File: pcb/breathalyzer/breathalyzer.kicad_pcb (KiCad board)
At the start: 2 copper layers, 37 parts, among them IC1 TPS3840DL25DBVR, J1 Conn_01x07_Pin, J2 MP-3B socket, Q1 Q_PMOS, Q2 NPN, SW1 PTS636SK43SMTR, SW2 430162085826, U1 STM32F030K6Tx, U2 TLV73325PDBV, U4 TLV61070ADBV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

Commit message: update from schematic
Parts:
- removed the R1 at (127.1, 108.4)
- added RV1: 50k_Potentiometer, Potentiometer_THT:Potentiometer_ACP_CA9-H5_Horizontal, F.Cu at (124.5, 109.3)
- SW2: value 430162085826 -> SW_Push_Dual
- moved SW2 5.24 mm to (215.3, 114.3)
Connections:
- SW2 pad 2: (no net) -> unconnected-(SW2-Pad2)
- SW2 pad 4: (no net) -> unconnected-(SW2-Pad4)

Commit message: net classes
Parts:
- moved J1 114.8 mm to (144.8, 188.0)
- moved U5 103.1 mm to (188.0, 55.9)
- moved BZ1 61.4 mm to (129.5, 175.3)
- moved U4 30.6 mm to (143.7, 132.6)
- moved R7 30.6 mm to (138.4, 131.9)
- moved L2 30.6 mm to (148.8, 132.1)
- moved DS1 24.0 mm to (151.1, 41.8)
- moved C10 11.2 mm to (160.2, 131.4)
- moved C11 11.2 mm to (160.2, 134.4)
- moved C9 11.2 mm to (160.0, 137.2)
- moved R6 11.2 mm to (160.0, 139.7)
- moved U1 8.09 mm to (148.6, 85.5)
- moved C4 3.36 mm to (138.9, 86.4)
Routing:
- net +2V5: track 0.00 -> 0.56 mm
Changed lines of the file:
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@@
 	(footprint "Capacitor_SMD:C_0603_1608Metric"
 		(layer "F.Cu")
-		(at 140.89 89.09)
+		(at 138.925 86.36)
 		(descr "Capacitor SMD 0603 (1608 Metric), square (rectangular) end terminal, IPC-7351 nominal, (Body size source: IPC-SM-782 page 76, https://www.pcb-3d.com/wordpress/wp-content/uploads/ipc-sm-782a_amendment_1_and_2.pdf), generated with kicad-footprint-generator")
 		(tags "capacitor")
@@
 	(footprint "Package_LCC:PLCC-44"
 		(layer "F.Cu")
-		(at 147.915 150.86)
+		(at 187.96 55.88)
 		(descr "PLCC, 44 pins, surface mount")
 		(tags "plcc smt")
@@
 	(footprint "Resistor_SMD:R_1206_3216Metric"
 		(layer "F.Cu")
-		(at 140.895 162.34)
+		(at 138.355 131.86)
 		(descr "Resistor SMD 1206 (3216 Metric), square (rectangular) end terminal, IPC-7351 nominal, (Body size source: IPC-SM-782 page 72, https://www.pcb-3d.com/wordpress/wp-content/uploads/ipc-sm-782a_amendment_1_and_2.pdf), generated with kicad-footprint-generator")
 		(tags "resistor")
@@
 	(footprint "Capacitor_SMD:C_0805_2012Metric"
 		(layer "F.Cu")
-		(at 159.965 142.54)
+		(at 160.24 131.39)
 		(descr "Capacitor SMD 0805 (2012 Metric), square (rectangular) end terminal, IPC-7351 nominal, (Body size source: IPC-SM-782 page 76, https://www.pcb-3d.com/wordpress/wp-content/uploads/ipc-sm-782a_amendment_1_and_2.pdf, https://docs.google.com/spreadsheets/d/1BsfQQcO9C6DZCsRaXUlFlo91Tg2WpOkGARC1WS5S8t0/edit?usp=sharing), generated with kicad-footprint-generator")
 		(tags "capacitor")
@@
 	(footprint "Capacitor_SMD:C_0603_1608Metric"
 		(layer "F.Cu")
-		(at 159.745 148.31)
+		(at 160.02 137.16)
 		(descr "Capacitor SMD 0603 (1608 Metric), square (rectangular) end terminal, IPC-7351 nominal, (Body size source: IPC-SM-782 page 76, https://www.pcb-3d.com/wordpress/wp-content/uploads/ipc-sm-782a_amendment_1_and_2.pdf), generated with kicad-footprint-generator")
 		(tags "capacitor")
@@
 	(footprint "breathalyzer:HDRRA7W66P0X254_1X7_1778X229X274P"
 		(layer "F.Cu")
-		(at 193.04 83.82)
+		(at 144.78 187.96)
 		(descr "22-28-8073")
 		(tags "Connector")
@@
 	(footprint "Package_TO_SOT_SMD:SOT-23-6"
 		(layer "F.Cu")
-		(at 146.275 163.085)
+		(at 143.735 132.605)
 		(descr "SOT, 6 Pin (JEDEC MO-178 Var AB https://www.jedec.org/document_search?search_api_views_fulltext=MO-178), generated with kicad-footprint-generator ipc_gullwing_generator.py")
 		(tags "SOT TO_SOT_SMD")
@@
 	(footprint "Capacitor_SMD:C_0805_2012Metric"
 		(layer "F.Cu")
-		(at 159.965 145.55)
+		(at 160.24 134.4)
 		(descr "Capacitor SMD 0805 (2012 Metric), square (rectangular) end terminal, IPC-7351 nominal, (Body size source: IPC-SM-782 page 76, https://www.pcb-3d.com/wordpress/wp-content/uploads/ipc-sm-782a_amendment_1_and_2.pdf, https://docs.google.com/spreadsheets/d/1BsfQQcO9C6DZCsRaXUlFlo91Tg2WpOkGARC1WS5S8t0/edit?usp=sharing), generated with kicad-footprint-generator")
 		(tags "capacitor")
@@
 	(footprint "breathalyzer:CPT1414680T"
 		(layer "F.Cu")
-		(at 182.88 144.78)
+		(at 129.54 175.26)
 		(descr "CPT-14146-80T-2")
 		(tags "Inductor")
@@
 	(footprint "Package_QFP:LQFP-32_7x7mm_P0.8mm"
 		(layer "F.Cu")
-		(at 148.6 93.54)
+		(at 148.6 85.455)
 		(descr "LQFP, 32 Pin (https://www.nxp.com/docs/en/package-information/SOT358-1.pdf), generated with kicad-footprint-generator ipc_gullwing_generator.py")
 		(tags "LQFP QFP")
@@
 	(footprint "breathalyzer:LCD-S301C31TR"
 		(layer "F.Cu")
-		(at 163.83 62.07)
+		(at 151.13 41.75)
 		(descr "LCD-S301C31TR")
 		(tags "Display")
@@
 	(footprint "Resistor_SMD:R_0603_1608Metric"
 		(layer "F.Cu")
-		(at 159.745 150.82)
+		(at 160.02 139.67)
 		(descr "Resistor SMD 0603 (1608 Metric), square (rectangular) end terminal, IPC-7351 nominal, (Body size source: IPC-SM-782 page 72, https://www.pcb-3d.com/wordpress/wp-content/uploads/ipc-sm-782a_amendment_1_and_2.pdf), generated with kicad-footprint-generator")
 		(tags "resistor")
@@
 	(footprint "Inductor_SMD:L_1008_2520Metric"
 		(layer "F.Cu")
-		(at 151.325 162.56)
+		(at 148.785 132.08)
 		(descr "Inductor SMD 1008 (2520 Metric), square (rectangular) end terminal, IPC-7351 nominal, (Body size source: https://ecsxtal.com/store/pdf/ECS-MPI2520-SMD-POWER-INDUCTOR.pdf), generated with kicad-footprint-generator")
 		(tags "inductor")
@@
 		)
 	)
+	(segment
+		(start 144.425 82.655)
+		(end 144.980918 82.655)
+		(width 0.2)
+		(layer "F.Cu")
+		(net 3)
+	)
 	(embedded_fonts no)

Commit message: +5V
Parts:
- removed C6: 1 uF, Capacitor_SMD:C_0603_1608Metric
- removed C7: 10 uF, Capacitor_SMD:C_0805_2012Metric
- removed IC1: TPS3840DL25DBVR, Package_TO_SOT_SMD:SOT-23-5_HandSoldering
- removed L1: 24 nH, Inductor_SMD:L_1008_2520Metric
- removed R1: 100k, Resistor_SMD:R_0402_1005Metric
- removed the R2 at (140.9, 96.6)
- removed R3: 56k, Resistor_SMD:R_0603_1608Metric
- removed the R4 at (138.2, 78.7)
- moved U2 72.4 mm to (208.1, 141.3)
- moved R7 56.2 mm to (193.0, 144.8), turned to -90 degrees
- moved U4 45.5 mm to (188.1, 142.6)
- moved L2 42.4 mm to (190.7, 138.4)
- moved R8 37.4 mm to (177.8, 151.1), turned to 180 degrees
- moved Q1 35.9 mm to (184.3, 151.1), turned to 90 degrees
- moved R6 32.1 mm to (190.5, 149.9)
- moved BT1 30.8 mm to (179.1, 147.3)
- moved C3 21.2 mm to (141.4, 82.5), turned to 180 degrees
- moved C1 18.5 mm to (142.0, 86.4), turned to 180 degrees
- moved C2 13.0 mm to (155.7, 88.9)
- moved R4 4.38 mm to (193.5, 122.0)
- moved R5 4.38 mm to (193.5, 124.5)
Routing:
- net +BATT: track 0.00 -> 24.7 mm
- net Net-(U4-V_{FB}): track 0.00 -> 9.27 mm
- net +2V5: track 0.56 -> 7.50 mm
- net Net-(U4-SW): track 0.00 -> 6.88 mm, vias 0 -> 2
- net Net-(BT1-+): track 0.00 -> 6.32 mm
- net Net-(Q1-G): track 0.00 -> 5.18 mm
- net +5V: track 0.00 -> 4.12 mm
- net GND: track 0.00 -> 3.85 mm

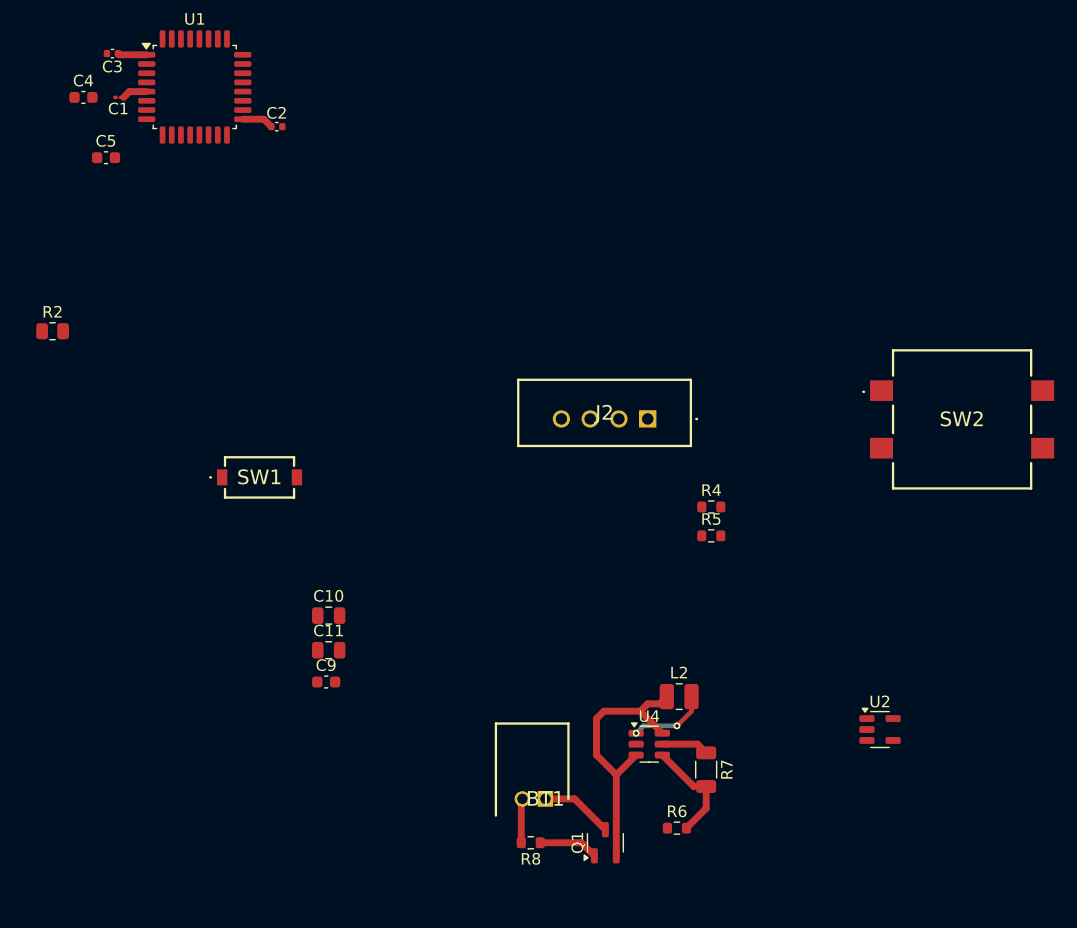
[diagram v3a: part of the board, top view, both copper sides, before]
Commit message: 5V fix
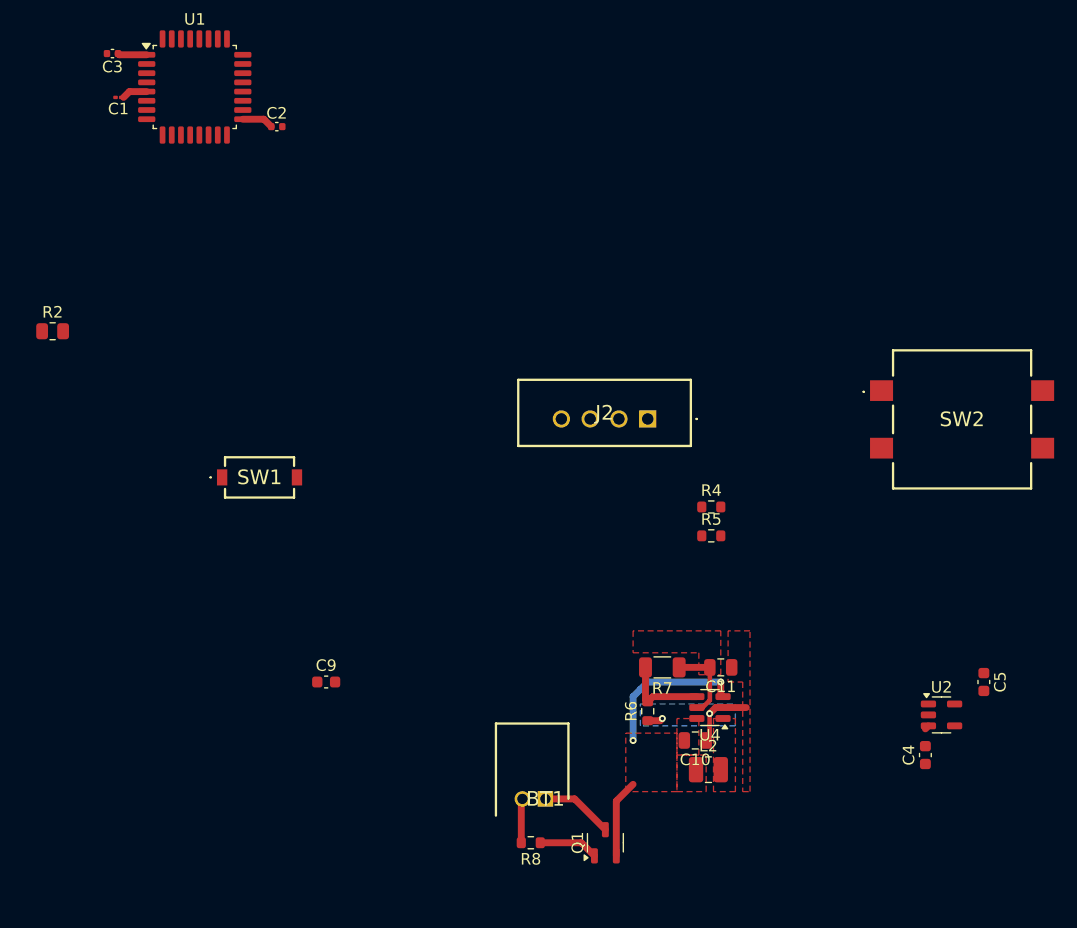
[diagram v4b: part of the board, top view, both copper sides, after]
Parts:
- moved C4 92.8 mm to (212.1, 143.5), turned to 90 degrees
- moved C5 88.9 mm to (217.2, 137.2), turned to -90 degrees
- moved C11 34.1 mm to (194.3, 135.9), turned to 180 degrees
- moved C10 33.6 mm to (192.1, 142.2), turned to 180 degrees
- moved R6 10.5 mm to (188.0, 139.7), turned to 90 degrees
- moved R7 9.67 mm to (189.2, 135.9), turned to 180 degrees
- moved L2 6.84 mm to (193.2, 144.8)
- moved U4 6.16 mm to (193.4, 139.4), turned to 180 degrees
- moved U2 5.49 mm to (213.5, 140.0)
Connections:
- C11 pad 1: Net-(U4-V_{FB}) -> GND
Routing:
- net GND: track 3.85 -> 11.1 mm, vias 0 -> 2
- net Net-(U4-SW): track 6.88 -> 0.00 mm, vias 2 -> 0
- net +BATT: track 24.7 -> 20.1 mm, vias 0 -> 2
- net +5V: track 4.12 -> 7.79 mm
- net Net-(U4-V_{FB}): track 9.27 -> 7.52 mm
- added copper zone on F.Cu, net +5V
- added copper zone on F.Cu, net +BATT
- added copper zone on B.Cu, net GND
- added copper zone on F.Cu, net GND
- added copper zone on F.Cu, net Net-(U4-SW)

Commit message: +2V5
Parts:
- moved C4 35.2 mm to (177.8, 135.8)
- moved C5 33.1 mm to (184.2, 135.8), turned to 90 degrees
- moved U2 32.6 mm to (181.1, 136.2)
- moved R4 23.8 mm to (169.7, 122.6)
- moved R5 23.8 mm to (169.7, 125.1)
- moved BT1 4.84 mm to (181.0, 142.9), turned to 90 degrees
- moved R8 3.17 mm to (180.3, 149.2), turned to 90 degrees
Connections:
- U2 pad 4: unconnected-(U2-NC-Pad4) -> GND
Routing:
- net +5V: track 7.79 -> 28.3 mm, vias 0 -> 2
- net Net-(BT1-+): track 6.32 -> 8.49 mm
- net Net-(Q1-G): track 5.18 -> 3.91 mm
- added copper zone on F.Cu, net +2V5

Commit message: pcb layout
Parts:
- BT1, BZ1, C1, C10, C11, C2, C3, C4, C5, J1, J2, L2, Q1, Q2, R2, R4, R5, R6, R7, R8, SW1, U1, U2, U4: moved to B.Cu
- moved BZ1 114.8 mm to (140.3, 61.0), turned to 180 degrees
- moved Q2 85.6 mm to (137.3, 41.9)
- moved J2 81.3 mm to (152.3, 41.3)
- moved J1 78.8 mm to (141.0, 109.2)
- moved Q1 71.9 mm to (138.4, 95.8), turned to -90 degrees
- moved R8 69.0 mm to (134.4, 97.7), turned to -90 degrees
- moved SW2 68.3 mm to (148.6, 99.7)
- moved RV1 62.9 mm to (155.7, 54.6)
- moved R2 62.6 mm to (133.3, 44.2), turned to -90 degrees
- moved L2 62.0 mm to (153.0, 97.6), turned to 90 degrees
- moved C9 59.2 mm to (136.1, 82.9)
- moved BT1 57.1 mm to (139.1, 104.0), turned to -90 degrees
- moved C10 56.8 mm to (155.6, 98.7), turned to -90 degrees
- moved R5 56.2 mm to (151.8, 71.8)
- moved U4 54.6 mm to (158.4, 97.5), turned to -90 degrees
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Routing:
- net LCD_A1: track 0.00 -> 57.1 mm
- net LCD_B1: track 0.00 -> 55.3 mm
- net LCD_G3: track 0.00 -> 48.5 mm
- net LCD_F1: track 0.00 -> 43.2 mm, vias 0 -> 1
- net LCD_F3: track 0.00 -> 42.1 mm
- net LCD_G2: track 0.00 -> 39.5 mm
- net LCD_F2: track 0.00 -> 35.9 mm
- net LCD_G1: track 0.00 -> 33.8 mm, vias 0 -> 1
- net ADC_IN: track 0.00 -> 33.3 mm, vias 0 -> 1
- net LCD_B3: track 0.00 -> 30.6 mm, vias 0 -> 1
- net LCD_B2: track 0.00 -> 30.6 mm
- net LCD_A3: track 0.00 -> 30.1 mm
- net LCD_A2: track 0.00 -> 30.1 mm
- net LCD_C1: track 0.00 -> 26.6 mm, vias 0 -> 1
- net LCD_E1: track 0.00 -> 26.4 mm, vias 0 -> 1
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- added copper zone on B.Cu, net +2V5
- added copper zone on B.Cu, net +5V
- added copper zone on B.Cu, net +BATT
- added copper zone on B.Cu, net Net-(U4-SW)
- removed copper zone on F.Cu, net +2V5
- removed copper zone on F.Cu, net +5V
- removed copper zone on F.Cu, net +BATT
- removed copper zone on F.Cu, net Net-(U4-SW)

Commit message: layout update
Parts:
- RV1: moved to B.Cu
- moved BZ1 60.6 mm to (158.8, 118.7)
- moved RV1 30.7 mm to (163.2, 84.5), turned to 180 degrees
- moved SW1 29.0 mm to (161.9, 74.9)
- moved C4 12.8 mm to (159.5, 100.5)
- moved C5 12.8 mm to (159.5, 94.2)
- moved U2 12.8 mm to (159.1, 97.2)
- moved C11 9.54 mm to (152.4, 96.1)
- moved L2 9.54 mm to (143.5, 97.2)
- moved R6 9.54 mm to (148.6, 102.4)
- moved R7 9.54 mm to (152.4, 101.2)
- moved U4 9.54 mm to (148.9, 97.0)
- moved C10 9.54 mm to (146.1, 98.3)
- moved J1 6.99 mm to (134.0, 109.2)
- moved BT1 1.08 mm to (139.1, 102.9)
- moved Q1 1.08 mm to (138.4, 94.7)
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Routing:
- net +5V: track 28.3 -> 7.41 mm, vias 2 -> 0

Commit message: layout update
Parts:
- moved C2 21.1 mm to (154.4, 53.9)
- moved R4 21.1 mm to (145.1, 64.1)
- moved C1 21.1 mm to (140.6, 56.5)
- moved C3 21.1 mm to (140.1, 60.3)
- moved U1 21.1 mm to (147.2, 57.4)
- moved R5 21.1 mm to (150.2, 50.8)
- moved SW1 1.83 mm to (161.9, 76.8)
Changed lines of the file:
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@@
 	(footprint "Resistor_SMD:R_0603_1608Metric"
 		(layer "B.Cu")
-		(at 146.735 85.185 180)
+		(at 145.135 64.1 180)
 		(descr "Resistor SMD 0603 (1608 Metric), square (rectangular) end terminal, IPC-7351 nominal, (Body size source: IPC-SM-782 page 72, https://www.pcb-3d.com/wordpress/wp-content/uploads/ipc-sm-782a_amendment_1_and_2.pdf), generated with kicad-footprint-generator")
 		(tags "resistor")
@@
 	(footprint "Capacitor_SMD:C_0402_1005Metric"
 		(layer "B.Cu")
-		(at 141.675 81.375 180)
+		(at 140.075 60.29 180)
 		(descr "Capacitor SMD 0402 (1005 Metric), square (rectangular) end terminal, IPC-7351 nominal, (Body size source: IPC-SM-782 page 76, https://www.pcb-3d.com/wordpress/wp-content/uploads/ipc-sm-782a_amendment_1_and_2.pdf), generated with kicad-footprint-generator")
 		(tags "capacitor")
@@
 	(footprint "Capacitor_SMD:C_0402_1005Metric"
 		(layer "B.Cu")
-		(at 155.955 75.025)
+		(at 154.355 53.94)
 		(descr "Capacitor SMD 0402 (1005 Metric), square (rectangular) end terminal, IPC-7351 nominal, (Body size source: IPC-SM-782 page 76, https://www.pcb-3d.com/wordpress/wp-content/uploads/ipc-sm-782a_amendment_1_and_2.pdf), generated with kicad-footprint-generator")
 		(tags "capacitor")
@@
 	(footprint "breathalyzer:PTS636SM43JSMTRLFS"
 		(layer "B.Cu")
-		(at 161.925 74.93 -90)
+		(at 161.925 76.76 -90)
 		(descr "PTS636SM43JSMTR LFS-1")
 		(tags "Switch")
@@
 	(footprint "Resistor_SMD:R_0603_1608Metric"
 		(layer "B.Cu")
-		(at 151.815 71.85)
+		(at 150.215 50.765)
 		(descr "Resistor SMD 0603 (1608 Metric), square (rectangular) end terminal, IPC-7351 nominal, (Body size source: IPC-SM-782 page 72, https://www.pcb-3d.com/wordpress/wp-content/uploads/ipc-sm-782a_amendment_1_and_2.pdf), generated with kicad-footprint-generator")
 		(tags "resistor")
@@
 	(footprint "Package_QFP:LQFP-32_7x7mm_P0.8mm"
 		(layer "B.Cu")
-		(at 148.825 78.47)
+		(at 147.225 57.385)
 		(descr "LQFP, 32 Pin (https://www.nxp.com/docs/en/package-information/SOT358-1.pdf), generated with kicad-footprint-generator ipc_gullwing_generator.py")
 		(tags "LQFP QFP")
@@
 	(footprint "Capacitor_SMD:C_01005_0402Metric"
 		(layer "B.Cu")
-		(at 142.19 77.565 180)
+		(at 140.59 56.48 180)
 		(descr "Capacitor SMD 01005 (0402 Metric), square (rectangular) end terminal, IPC-7351 nominal, (Body size source: http://www.vishay.com/docs/20056/crcw01005e3.pdf), generated with kicad-footprint-generator")
 		(tags "capacitor")
@@
 	)
 	(segment
-		(start 152.64 73.28)
-		(end 151.625 74.295)
+		(start 151.04 52.195)
+		(end 150.025 53.21)
 		(width 0.6)
 		(layer "B.Cu")
@@
 	)
 	(segment
-		(start 152.64 71.85)
-		(end 152.64 73.28)
+		(start 151.04 50.765)
+		(end 151.04 52.195)
 		(width 0.6)
 		(layer "B.Cu")
@@
 	)
 	(segment
-		(start 145.91 82.76)
-		(end 146.025 82.645)
+		(start 144.31 61.675)
+		(end 144.425 61.56)
 		(width 0.6)
 		(layer "B.Cu")
@@
 	)
 	(segment
-		(start 145.91 85.185)
-		(end 145.91 82.76)
+		(start 144.31 64.1)
+		(end 144.31 61.675)
 		(width 0.6)
 		(layer "B.Cu")
@@
 	)
 	(segment
-		(start 153 75.67)
-		(end 154.83 75.67)
+		(start 151.4 54.585)
+		(end 153.23 54.585)
 		(width 0.6)
 		(layer "B.Cu")
@@
 	)
 	(segment
-		(start 143.146 78.07)
-		(end 142.641 77.565)
+		(start 141.546 56.985)
+		(end 141.041 56.48)
 		(width 0.6)
 		(layer "B.Cu")
@@
 	)
 	(segment
-		(start 144.65 81.27)
-		(end 142.26 81.27)
+		(start 143.05 60.185)
+		(end 140.66 60.185)
 		(width 0.6)
 		(layer "B.Cu")
@@
 	)
 	(segment
-		(start 154.83 75.67)
-		(end 155.475 75.025)
+		(start 153.23 54.585)
+		(end 153.875 53.94)
 		(width 0.6)
 		(layer "B.Cu")
@@
 	)
 	(segment
-		(start 142.26 81.27)
-		(end 142.155 81.375)
-		(width 0.6)
-		(layer "B.Cu")
-		(net 3)
-	)
-	(segment
-		(start 144.65 78.07)
-		(end 143.146 78.07)
+		(start 143.05 56.985)
+		(end 141.546 56.985)
 		(width 0.6)
 		(layer "B.Cu")
@@
 	)
 	(segment
-		(start 150.825 72.015)
-		(end 150.825 74.295)
+		(start 149.225 50.93)
+		(end 149.225 53.21)
 		(width 0.4)
 		(layer "B.Cu")
@@
 	)
 	(segment
-		(start 147.56 85.185)
-		(end 146.825 84.45)
+		(start 145.96 64.1)
+		(end 145.225 63.365)
 		(width 0.4)
 		(layer "B.Cu")
@@
 	)
 	(segment
-		(start 146.825 84.45)
-		(end 146.825 82.645)
+		(start 145.225 63.365)
+		(end 145.225 61.56)
 		(width 0.4)
 		(layer "B.Cu")
